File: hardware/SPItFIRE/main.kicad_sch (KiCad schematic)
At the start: 35 parts, among them J1 Joystick A, J10 Peripheral User Port, J11 SPI_5, J12 SPI_6, J13 SPI_7, J2 Compact Host, J3 Joystick B, J4 User Port Host, J5 ISP, J6 SD Card Adapter, J7 Peripheral DE-9, J8 DeadOnRTC, J9 SPI_4, U1 74HC138, U2 ATmega1284P-A, Y1 Crystal

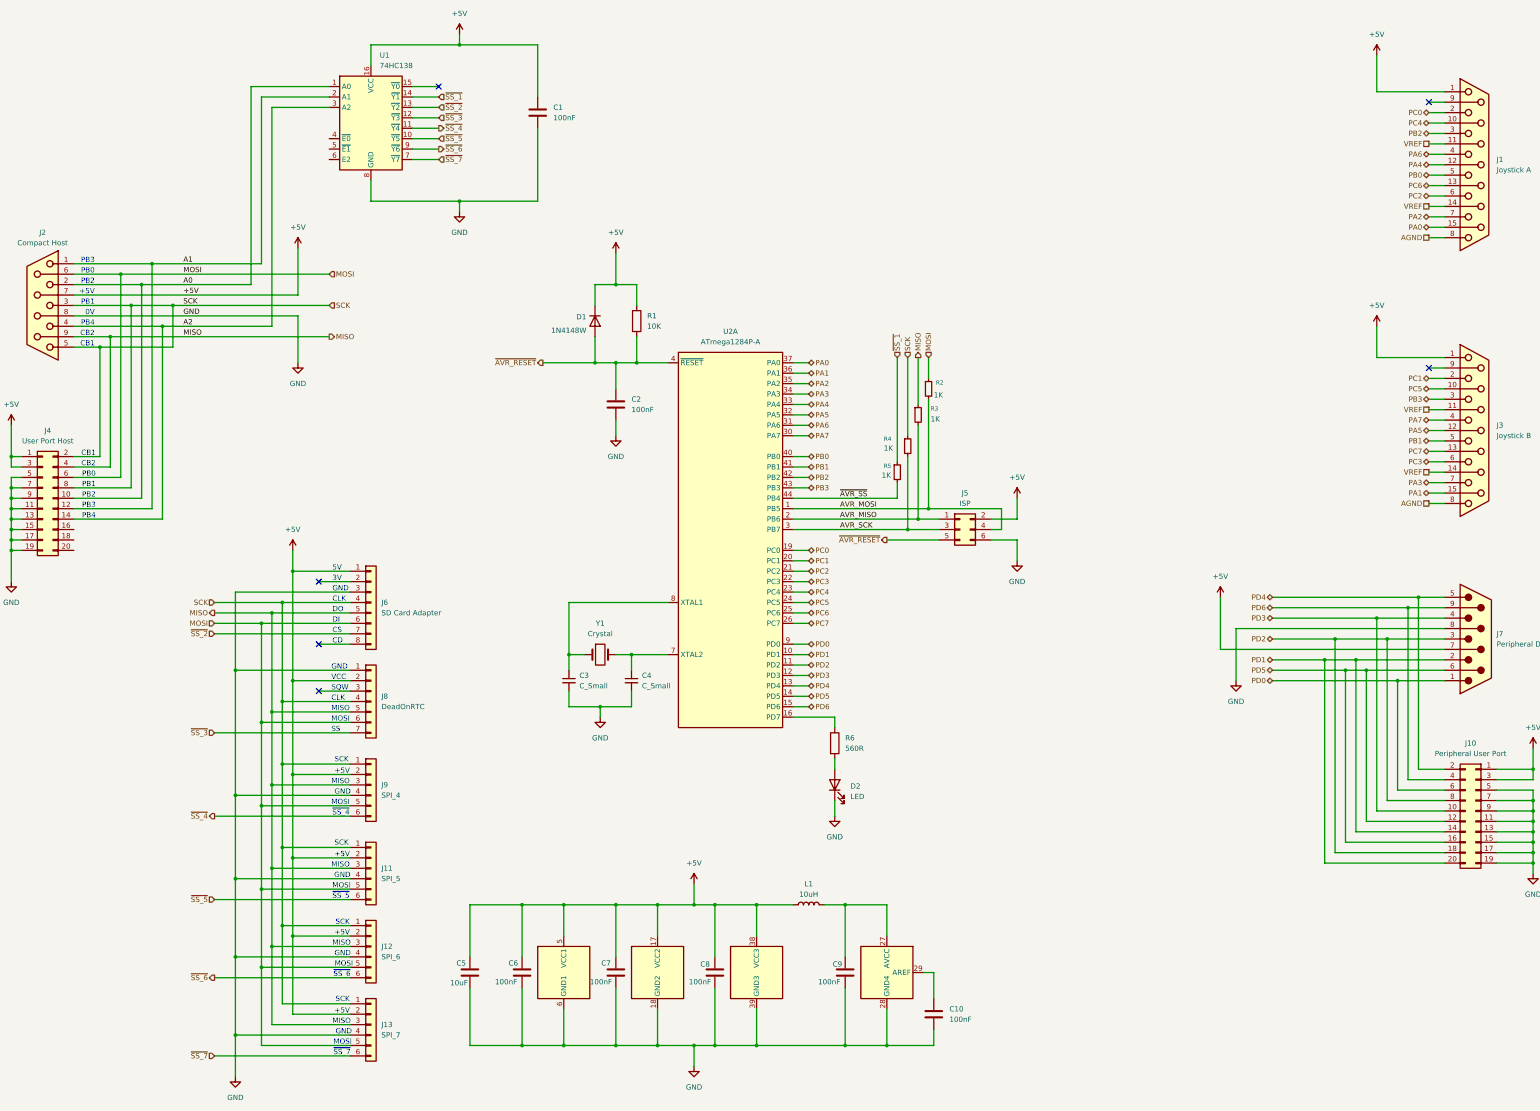
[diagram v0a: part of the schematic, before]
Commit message: Schematic updates
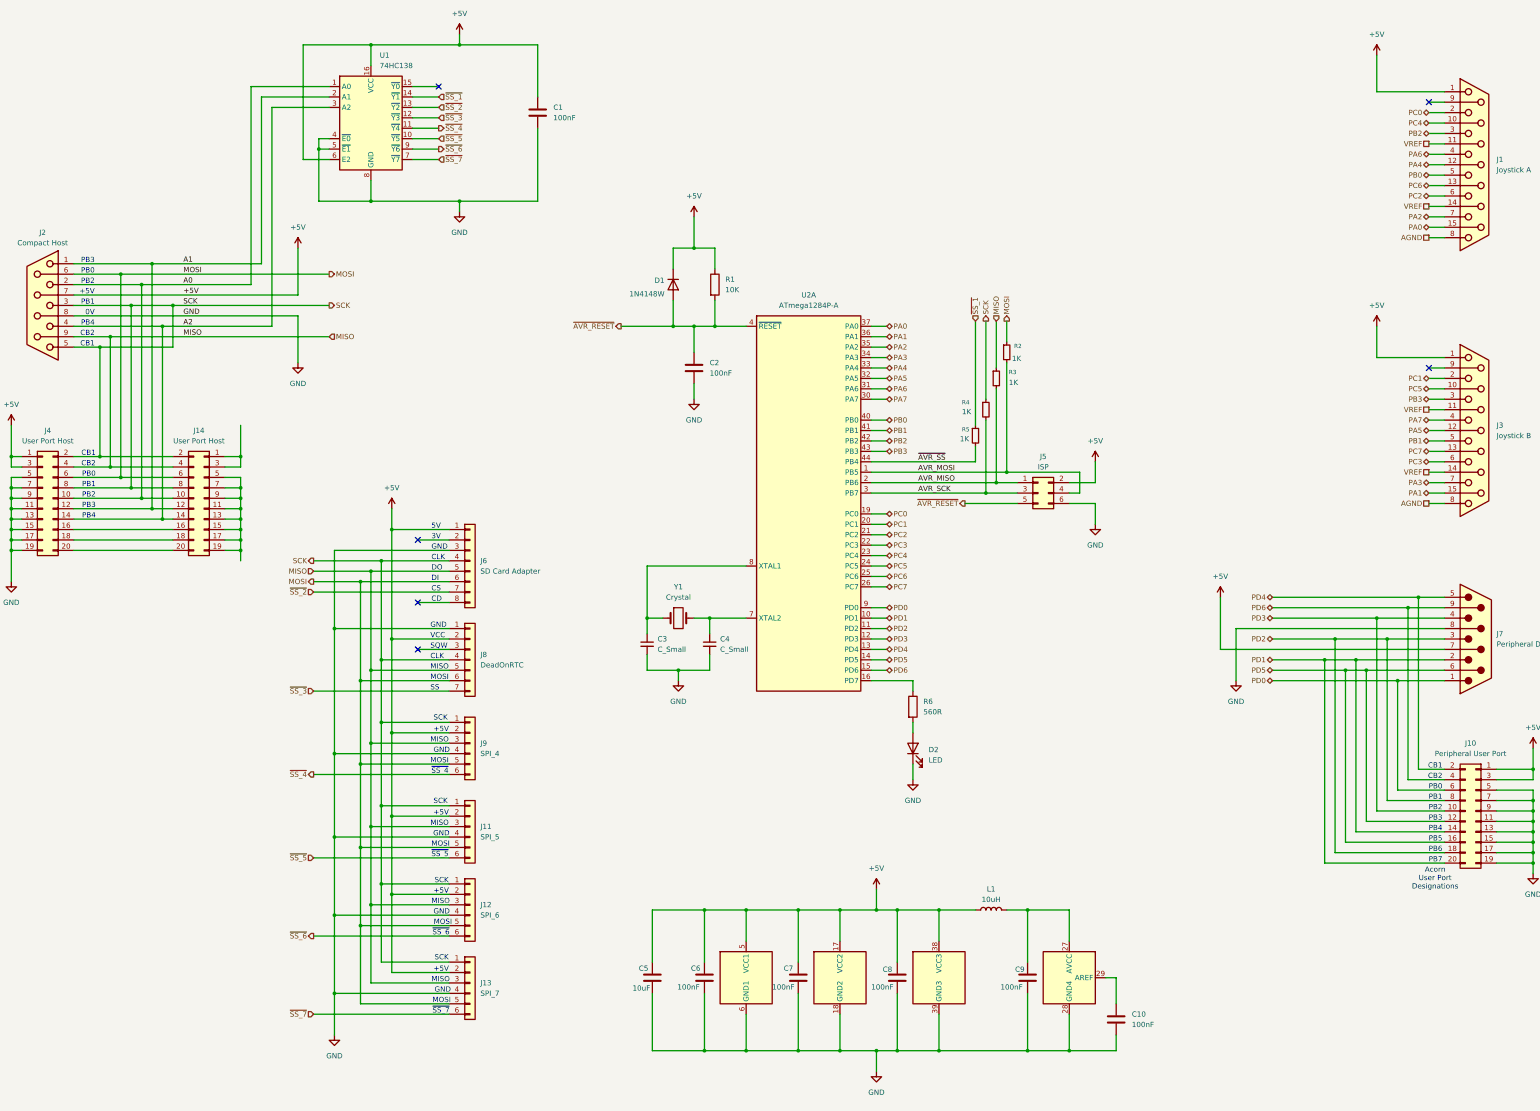
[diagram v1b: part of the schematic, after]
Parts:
- added J14: User Port Host, symbol Connector_Generic:Conn_02x10_Odd_Even
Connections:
- net +5V: now also U1.6 (E2)
- net A0: now also J14.10 (Pin_10)
- net A1: now also J14.12 (Pin_12)
- net A2: now also J14.14 (Pin_14)
- net GND: now also U1.4 (~{E0}), U1.5 (~{E1})
- net MISO: now also J14.4 (Pin_4)
- net MOSI: now also J14.6 (Pin_6)
- net SCK: now also J14.2 (Pin_2), J14.8 (Pin_8)
- net at J4.16 (Pin_16): now also J14.16 (Pin_16)
- net at J4.18 (Pin_18): now also J14.18 (Pin_18)
- net at J4.20 (Pin_20): now also J14.20 (Pin_20)
- new net: J14.1 (Pin_1), J14.3 (Pin_3)
- new net: J14.11 (Pin_11), J14.13 (Pin_13), J14.15 (Pin_15), J14.17 (Pin_17), J14.19 (Pin_19), J14.5 (Pin_5), J14.7 (Pin_7), J14.9 (Pin_9)
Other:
- note added: "Acorn User Port Designations"
- note added: "PB5"
- note added: "PB6"
- note added: "PB7"
- title: (none) -> SPItFIRE BBC Master Compact Joystick / Mouse interface
- moved on the sheet: C10, C2, C3, C4, C5, C6, C7, C8, C9, D1, D2, J11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

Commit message: Schematic updates and rule checking
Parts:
- J3: renamed from J14; value User Port Host -> User Port Passthrough
- renumbered C3 to C2, C5 to C3, C2 to C4, C6 to C5, C4 to C6, J2 to J1, J5 to J10, J1 to J11, J3 to J12, J7 to J13, J10 to J14, J4 to J2, J6 to J4, J8 to J5, J9 to J6, J11 to J7, J12 to J8, J13 to J9, R6 to R2, R5 to R3, R3 to R5, R2 to R6
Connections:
- net +5V: now also J3.1 (Pin_1), J3.3 (Pin_3)
- net GND: now also J3.11 (Pin_11), J3.13 (Pin_13), J3.15 (Pin_15), J3.17 (Pin_17), J3.19 (Pin_19), J3.5 (Pin_5), J3.7 (Pin_7), J3.9 (Pin_9)

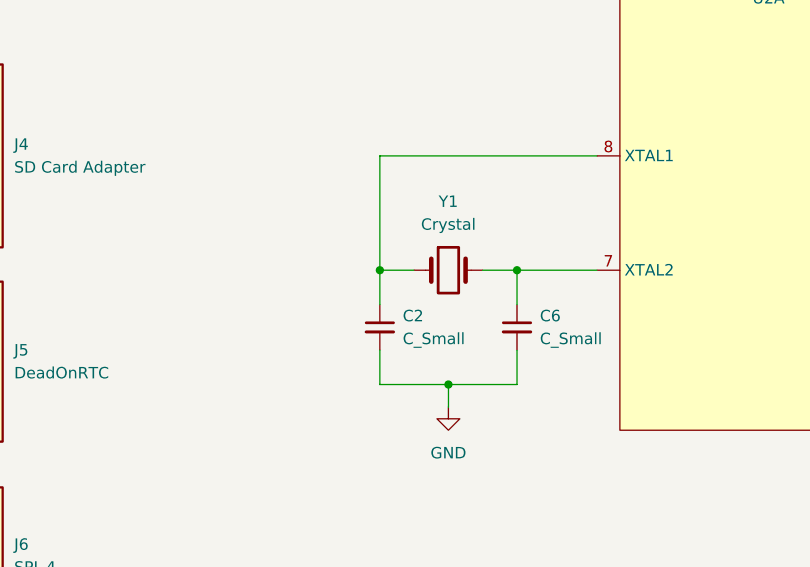
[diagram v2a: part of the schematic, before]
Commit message: Work on the schematic and the beginnings of footprint assignment
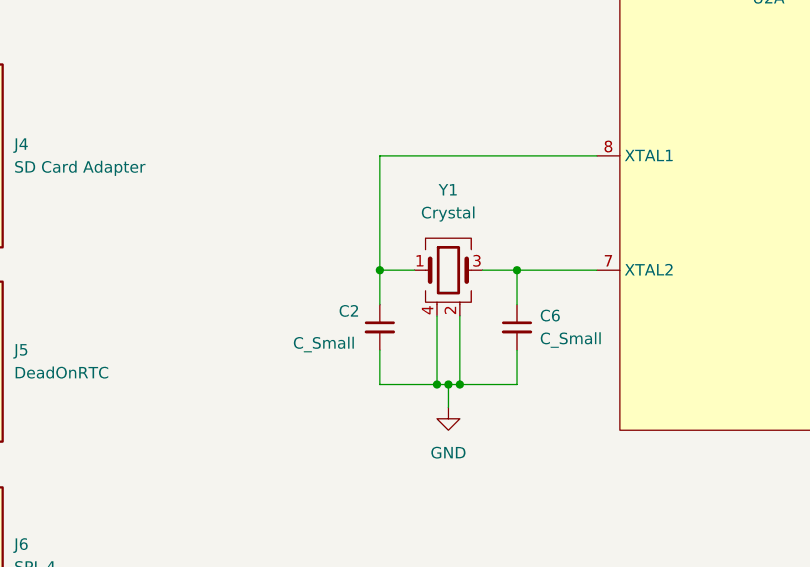
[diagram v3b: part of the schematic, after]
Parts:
- J1: footprint (none) -> SPItFIRE:DE9_Female_Horizontal_P2.74x2.84mm_EdgePinOffset10.40mm_Housed_MountingHolesOffset12.5mm
- J10, U1: footprint (none) -> Package_SO:SOIC-16_3.9x9.9mm_P1.27mm
- J11, J12: footprint (none) -> SPItFIRE:DA15_Female_Horizontal_P2.74x2.84mm_EdgePinOffset10.40mm_Housed_MountingHolesOffset16.66mm
- J13: footprint (none) -> SPItFIRE:DE9_Male_Horizontal_P2.74x2.84mm_EdgePinOffset10.40mm_Housed_MountingHolesOffset12.5mm_1
- J14, J2: footprint (none) -> Connector_PinHeader_2.54mm:PinHeader_2x10_P2.54mm_Horizontal
- J3: footprint (none) -> Connector_PinHeader_2.54mm:PinHeader_2x10_P2.54mm_Vertical
- J4: footprint (none) -> Connector_PinSocket_2.54mm:PinSocket_1x08_P2.54mm_Vertical
- J5: footprint (none) -> Connector_PinSocket_2.54mm:PinSocket_1x07_P2.54mm_Vertical
- J6, J7, J8, J9: footprint (none) -> Connector_PinSocket_2.54mm:PinSocket_1x06_P2.54mm_Vertical
- Y1: footprint (none) -> Crystal:Crystal_SMD_5032-4Pin_5.0x3.2mm; symbol Device:Crystal -> SPItFIRE:Crystal_GND24
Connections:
- net GND: now also Y1.2 (G), Y1.4 (G)
- net at C6.1, U2.7 (XTAL2): now also Y1.3; no longer Y1.2
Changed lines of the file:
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@@
 	)
 	(junction
+		(at 181.61 177.8)
+		(diameter 0)
+		(color 0 0 0 0)
+	)
+	(junction
 		(at 107.95 175.26)
 		(diameter 0)
@@
 	)
 	(junction
+		(at 179.07 177.8)
+		(diameter 0)
+		(color 0 0 0 0)
+	)
+	(junction
 		(at 265.43 270.51)
 		(diameter 0)
@@
 	(wire
 		(pts
+			(xy 181.61 177.8) (xy 187.96 177.8)
+		)
+		(stroke
+			(width 0)
+			(type default)
+		)
+	)
+	(wire
+		(pts
 			(xy 184.15 165.1) (xy 187.96 165.1)
 		)
@@
 	(wire
 		(pts
-			(xy 172.72 177.8) (xy 180.34 177.8)
+			(xy 172.72 177.8) (xy 179.07 177.8)
 		)
 		(stroke
@@
 	(wire
 		(pts
+			(xy 179.07 170.18) (xy 179.07 177.8)
+		)
+		(stroke
+			(width 0)
+			(type default)
+		)
+	)
+	(wire
+		(pts
 			(xy 379.73 217.17) (xy 388.62 217.17)
 		)
@@
 	(wire
 		(pts
+			(xy 179.07 177.8) (xy 180.34 177.8)
+		)
+		(stroke
+			(width 0)
+			(type default)
+		)
+	)
+	(wire
+		(pts
 			(xy 388.62 196.85) (xy 388.62 201.93)
 		)
@@
 	(wire
 		(pts
-			(xy 180.34 177.8) (xy 187.96 177.8)
+			(xy 180.34 177.8) (xy 181.61 177.8)
 		)
 		(stroke
@@
 	(wire
 		(pts
+			(xy 181.61 170.18) (xy 181.61 177.8)
+		)
+		(stroke
+			(width 0)
+			(type default)
+		)
+	)
+	(wire
+		(pts
 			(xy 275.59 270.51) (xy 275.59 261.62)
 		)
@@
 			)
 		)
-		(property "Footprint" ""
+		(property "Footprint" "Connector_PinSocket_2.54mm:PinSocket_1x06_P2.54mm_Vertical"
 			(at 129.54 195.58 0)
 			(hide yes)
@@
 			)
 		)
-		(property "Footprint" ""
+		(property "Footprint" "Connector_PinHeader_2.54mm:PinHeader_2x10_P2.54mm_Horizontal"
 			(at 25.4 135.89 0)
 			(hide yes)
@@
 			)
 		)
-		(property "Footprint" ""
+		(property "Footprint" "SPItFIRE:DE9_Male_Horizontal_P2.74x2.84mm_EdgePinOffset10.40mm_Housed_MountingHolesOffset12.5mm_1"
 			(at 374.65 170.18 0)
 			(hide yes)
@@
 			)
 		)
-		(property "Footprint" ""
+		(property "Footprint" "SPItFIRE:DA15_Female_Horizontal_P2.74x2.84mm_EdgePinOffset10.40mm_Housed_MountingHolesOffset16.66mm"
 			(at 374.65 54.61 0)
 			(hide yes)
@@
 			)
 		)
-		(property "Footprint" ""
+		(property "Footprint" "Connector_PinHeader_2.54mm:PinHeader_2x10_P2.54mm_Horizontal"
 			(at 374.65 212.09 0)
 			(hide yes)
@@
 		(in_pos_files yes)
 		(dnp no)
-		(fields_autoplaced yes)
 		(property "Reference" "C2"
-			(at 175.26 170.1862 0)
+			(at 168.148 169.672 0)
 			(show_name no)
 			(do_not_autoplace no)
@@
 		)
 		(property "Value" "C_Small"
-			(at 175.26 172.7262 0)
+			(at 163.068 173.228 0)
 			(show_name no)
 			(do_not_autoplace no)
@@
 			)
 		)
-		(property "Footprint" ""
+		(property "Footprint" "Connector_PinSocket_2.54mm:PinSocket_1x06_P2.54mm_Vertical"
 			(at 129.54 234.95 0)
 			(hide yes)
@@
 			)
 		)
-		(property "Footprint" ""
+		(property "Footprint" "SPItFIRE:DA15_Female_Horizontal_P2.74x2.84mm_EdgePinOffset10.40mm_Housed_MountingHolesOffset16.66mm"
 			(at 374.65 119.38 0)
 			(hide yes)
@@
 			)
 		)
-		(property "Footprint" ""
+		(property "Footprint" "Connector_PinSocket_2.54mm:PinSocket_1x08_P2.54mm_Vertical"
 			(at 129.54 151.13 0)
 			(hide yes)
@@
 			)
 		)
-		(property "Footprint" ""
+		(property "Footprint" "Connector_PinHeader_2.54mm:PinHeader_2x10_P2.54mm_Vertical"
 			(at 64.77 135.89 0)
 			(hide yes)
@@
 			)
 		)
-		(property "Footprint" ""
+		(property "Footprint" "Connector_PinSocket_2.54mm:PinSocket_1x06_P2.54mm_Vertical"
 			(at 129.54 215.9 0)
 			(hide yes)
@@
 			)
 		)
-		(property "Footprint" ""
+		(property "Footprint" "SPItFIRE:DE9_Female_Horizontal_P2.74x2.84mm_EdgePinOffset10.40mm_Housed_MountingHolesOffset12.5mm"
 			(at 25.4 88.9 0)
 			(hide yes)
@@
 	)
 	(symbol
-		(lib_id "Device:Crystal")
+		(lib_id "SPItFIRE:Crystal_GND24")
 		(at 180.34 165.1 0)
 		(unit 1)
@@
 		(fields_autoplaced yes)
 		(property "Reference" "Y1"
-			(at 180.34 157.48 0)
+			(at 180.34 156.21 0)
 			(show_name no)
 			(do_not_autoplace no)
@@
 		)
 		(property "Value" "Crystal"
-			(at 180.34 160.02 0)
+			(at 180.34 158.75 0)
 			(show_name no)
 			(do_not_autoplace no)
@@
 			)
 		)
-		(property "Footprint" ""
+		(property "Footprint" "Crystal:Crystal_SMD_5032-4Pin_5.0x3.2mm"
 			(at 180.34 165.1 0)
 			(hide yes)
@@
 			)
 		)
-		(property "Description" "Two pin crystal"
+		(property "Description" "Four pin crystal, GND on pins 2 and 4"
 			(at 180.34 165.1 0)
 			(hide yes)
@@
 		(pin "2"
 		)
+		(pin "4"
+		)
+		(pin "3"
+		)
 		(instances
 			(project "SPItFIRE"
@@
 			)
 		)
-		(property "Footprint" ""
+		(property "Footprint" "Package_SO:SOIC-16_3.9x9.9mm_P1.27mm"
 			(at 105.41 45.72 0)
 			(hide yes)
@@
 			)
 		)
-		(property "Footprint" ""
+		(property "Footprint" "Connector_PinSocket_2.54mm:PinSocket_1x07_P2.54mm_Vertical"
 			(at 129.54 175.26 0)
 			(hide yes)
@@
 			)
 		)
-		(property "Footprint" ""
+		(property "Footprint" "Package_SO:SOIC-16_3.9x9.9mm_P1.27mm"
 			(at 267.97 134.62 0)
 			(hide yes)
@@
 			)
 		)
-		(property "Footprint" ""
+		(property "Footprint" "Connector_PinSocket_2.54mm:PinSocket_1x06_P2.54mm_Vertical"
 			(at 129.54 254 0)
 			(hide yes)
